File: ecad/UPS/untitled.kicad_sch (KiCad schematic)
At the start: 10 parts, among them U1 BQ25731RSNR

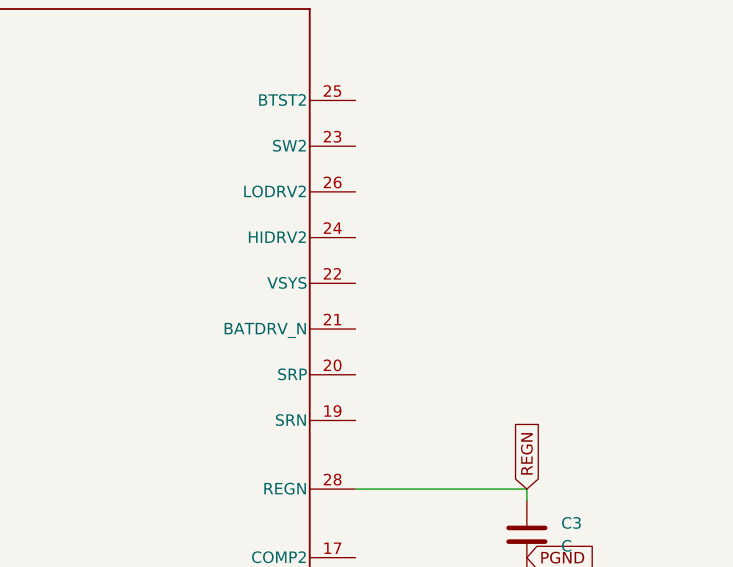
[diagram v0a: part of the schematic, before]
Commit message: Made Buck Convertor Schematic
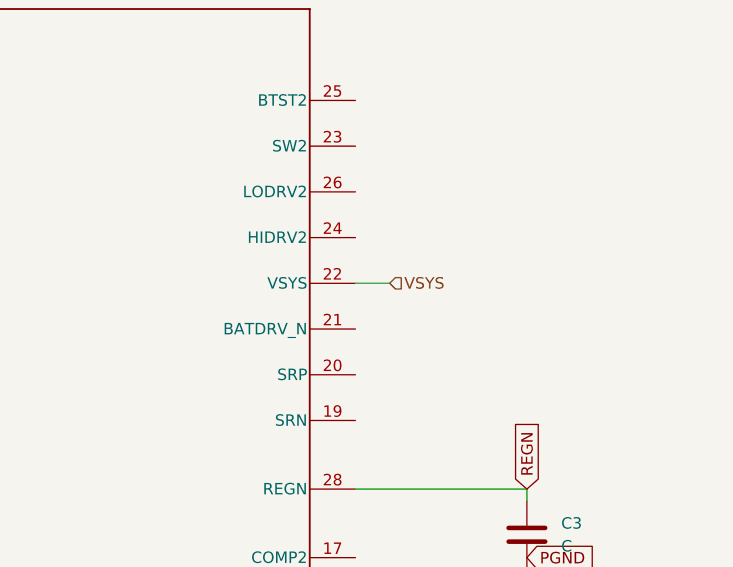
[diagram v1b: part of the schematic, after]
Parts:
- U1: footprint RSN0032B-IPC_A -> UPS:RSN0032B-IPC_A
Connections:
- net VSYS: now reaches U1.22 (VSYS)
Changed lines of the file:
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@@
+	(wire
+		(pts
+			(xy 172.72 68.58) (xy 168.91 68.58)
+		)
+		(stroke
+			(width 0)
+			(type default)
+		)
+	)
 	(wire
 		(pts
@@
 		)
 	)
+	(hierarchical_label "VSYS"
+		(shape input)
+		(at 172.72 68.58 0)
+		(effects
+			(font
+				(size 1.27 1.27)
+			)
+			(justify left)
+		)
+	)
 	(symbol
 		(lib_id "Device:C")
@@
 			)
 		)
-		(property "Footprint" "RSN0032B-IPC_A"
+		(property "Footprint" "UPS:RSN0032B-IPC_A"
 			(at 115.57 43.18 0)
 			(effects

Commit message: First half of BQ schematic
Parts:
- added C13, C14, C15, C16, C17: C, symbol Device:C
- added L1: L, symbol Device:L
- added Q1, Q2, Q3, Q4: NMOS, symbol Simulation_SPICE:NMOS
- added R10, R11, R9: R, symbol Device:R
- U1: footprint UPS:RSN0032B-IPC_A -> RSN0032B-IPC_A
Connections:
- net GND: now also C13.2, C15.1, Q2.3 (S), Q3.3 (S)
- net VBUS_IN: now also R10.2, R11.2
- net at U1.2 (ACN): now also C13.1, C14.2, R9.1
- net at U1.23 (SW2): now also C17.2, L1.2, Q3.1 (D), Q4.3 (S)
- net at U1.24 (HIDRV2): now also Q4.2 (G)
- net BTST2: now reaches U1.25 (BTST2)
- net BTST2: now also C17.1
- net at U1.26 (LODRV2): now also Q3.2 (G)
- net at U1.29 (LODRV1): now also Q2.2 (G)
- net at U1.3 (ACP): now also C14.1, C15.2, R10.1
- net BTST1: now reaches U1.30 (BTST1)
- net BTST1: now also C16.1
- net at U1.31 (HIDRV1): now also Q1.2 (G)
- net VSYS: no longer names the net of U1.22 (VSYS)
- net VSYS: now also Q4.1 (D)
- new net: C16.2, L1.1, Q1.3 (S), Q2.1 (D)
- new net: Q1.1 (D), R11.1, R9.2
